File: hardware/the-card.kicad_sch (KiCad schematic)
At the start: 75 parts, among them J1 TYPE-C-31-M-12, J2 FH12-24S-0.5SH(55), J3 S2B-PH-SM4-TB(LF)(SN), Q1 SI2301CDS-T1-GE3, Q2 SI2301CDS-T1-GE3, Q3 SI1308EDL-T1-GE3, SW1 TS-1187A-B-A-B, SW2 TS-1187A-B-A-B, SW3 TS-1187A-B-A-B, SW4 TS-1187A-B-A-B, U1 ESP32-S3-WROOM-1-N16R8, U10 USBLC6-2SC6, U2 ST25DV04KC-IE8S3, U3 LSM6DSOTR, U4 SHT40-BD1B-R2, U5 MAX17048G+T10, U6 TP4056_C382139, U7 DW01A_C18164398, U8 8205A, U9 ME6211C33M5G-N

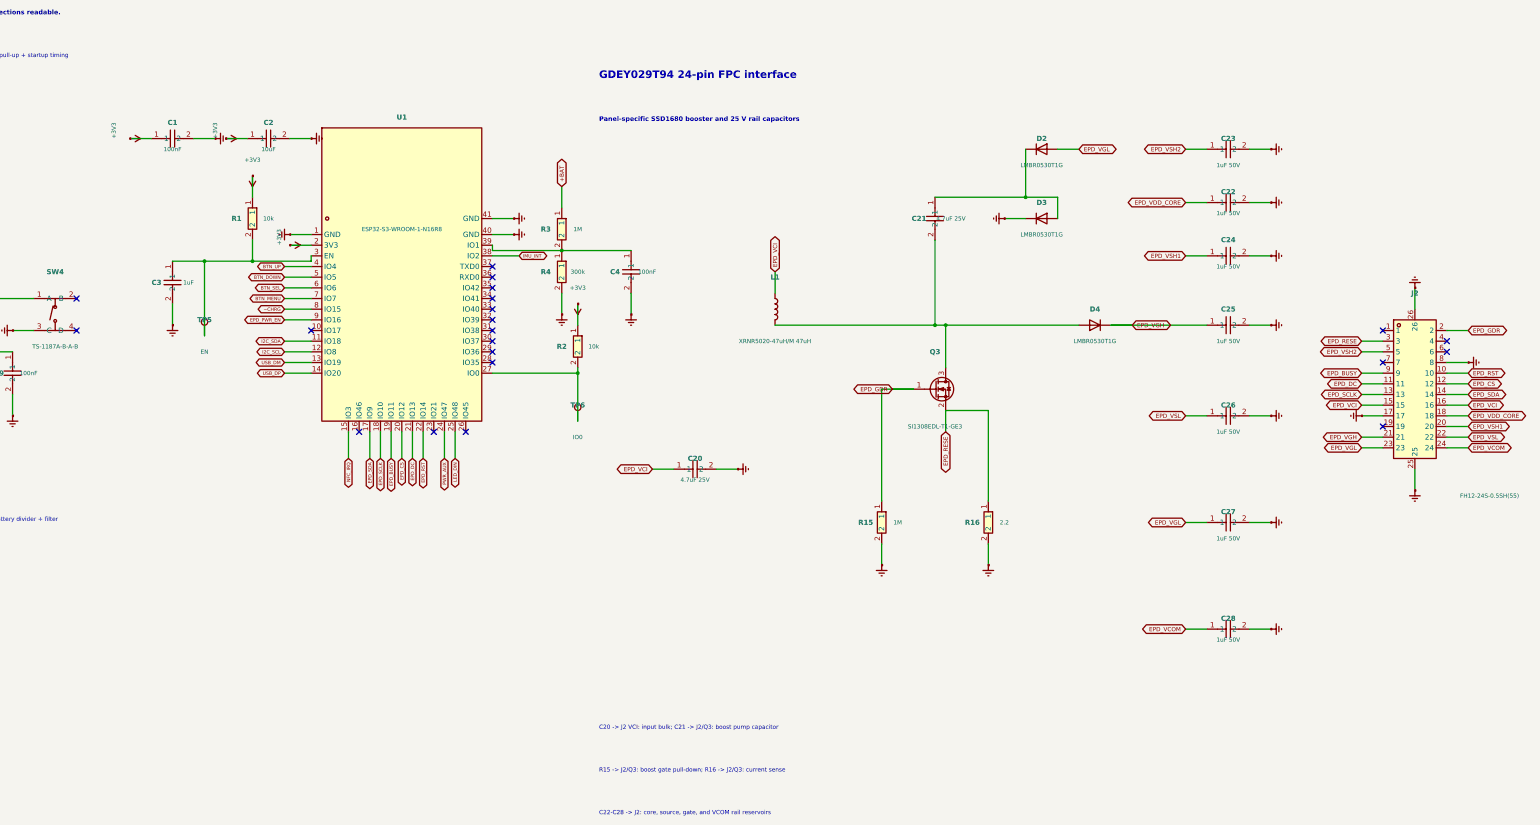
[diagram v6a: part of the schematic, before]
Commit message: refactor(hardware): clarify schematic component groups
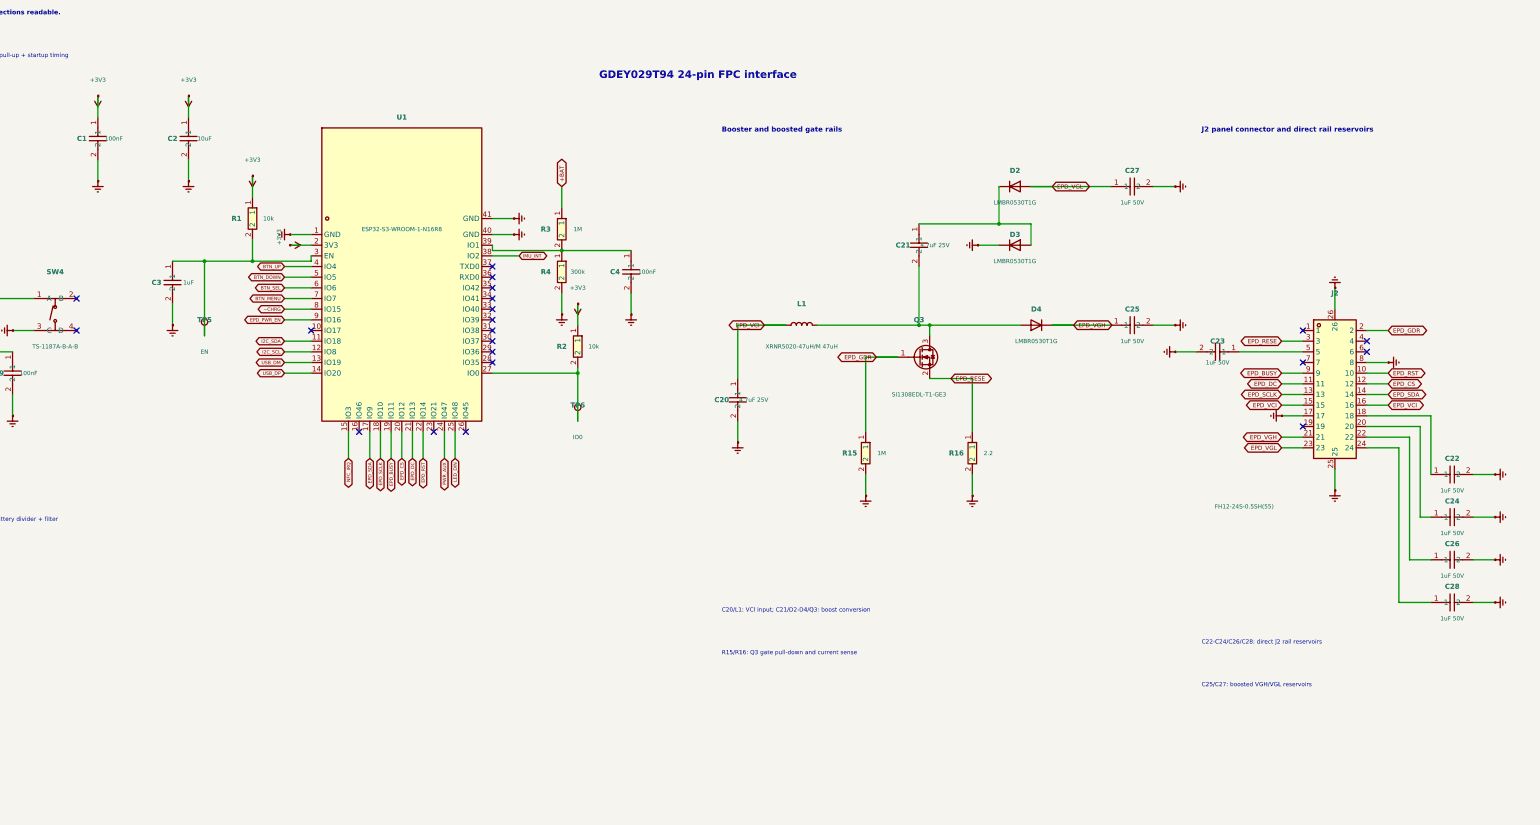
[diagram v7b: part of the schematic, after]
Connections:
- net EPD_VCOM: no longer names the net of C28.1, J2.24
- net EPD_VDD_CORE: no longer names the net of C22.1, J2.18
- net EPD_VSH1: no longer names the net of C24.1, J2.20
- net EPD_VSH2: no longer names the net of C23.1, J2.5
- net EPD_VSL: no longer names the net of C26.1, J2.22
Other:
- note added: "Booster and boosted gate rails"
- note added: "C20/L1: VCI input; C21/D2-D4/Q3: boost conversion"
- note added: "C22-C24/C26/C28: direct J2 rail reservoirs"
- note added: "C25/C27: boosted VGH/VGL reservoirs"
- note added: "J2 panel connector and direct rail reservoirs"
- note added: "R15/R16: Q3 gate pull-down and current sense"
- note removed: "C20 -> J2 VCI: input bulk; C21 -> J2/Q3: boost pump capacitor"
- note removed: "C22-C28 -> J2: core, source, gate, and VCOM rail reservoirs"
- note removed: "Panel-specific SSD1680 booster and 25 V rail capacitors"
- note removed: "R15 -> J2/Q3: boost gate pull-down; R16 -> J2/Q3: current sense"
- moved on the sheet: C1, C2, C20, C21, C22, C23, C24, C25, C26, C27, C28, D2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
